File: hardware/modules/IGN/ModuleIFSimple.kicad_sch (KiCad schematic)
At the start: 4 parts, among them J401 Jumper, J402 Conn_01x04_MountingPin

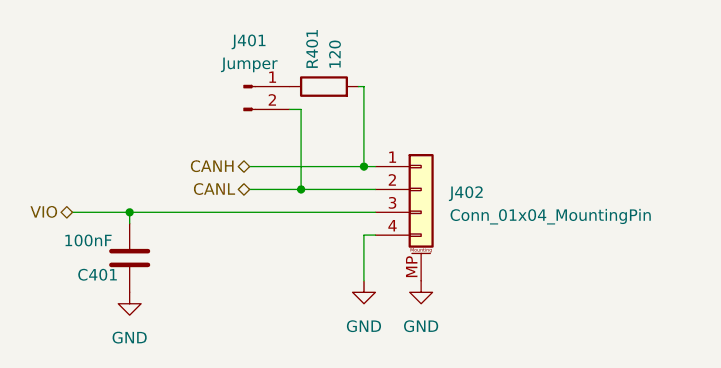
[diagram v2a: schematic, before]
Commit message: CAN周り終端抵抗の位置とか一部変更
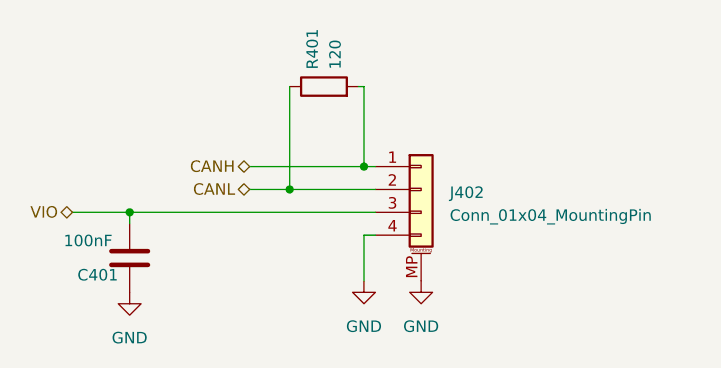
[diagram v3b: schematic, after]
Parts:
- removed J401: Jumper, Connector_PinHeader_1.27mm:PinHeader_1x02_P1.27mm_Vertical, symbol Connector:Conn_01x02_Pin
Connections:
- net CANL: now also R401.1
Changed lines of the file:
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@@
+	)
+	(junction
+		(at 172.72 66.04)
+		(diameter 0)
+		(color 0 0 0 0)
 	)
 	(junction
@@
 		(color 0 0 0 0)
 	)
-	(junction
-		(at 173.99 66.04)
-		(diameter 0)
-		(color 0 0 0 0)
-	)
 	(wire
 		(pts
@@
 	(wire
 		(pts
-			(xy 173.99 57.15) (xy 173.99 66.04)
-		)
-		(stroke
-			(width 0)
-			(type default)
-		)
-	)
-	(wire
-		(pts
 			(xy 154.94 68.58) (xy 182.245 68.58)
 		)
@@
 	(wire
 		(pts
-			(xy 173.99 66.04) (xy 182.245 66.04)
-		)
-		(stroke
-			(width 0)
-			(type default)
-		)
-	)
-	(wire
-		(pts
 			(xy 154.94 68.58) (xy 154.94 69.85)
 		)
@@
 	(wire
 		(pts
+			(xy 172.72 66.04) (xy 182.245 66.04)
+		)
+		(stroke
+			(width 0)
+			(type default)
+		)
+	)
+	(wire
+		(pts
 			(xy 182.245 71.12) (xy 180.975 71.12)
 		)
@@
 	(wire
 		(pts
-			(xy 168.275 66.04) (xy 173.99 66.04)
-		)
-		(stroke
-			(width 0)
-			(type default)
-		)
-	)
-	(wire
-		(pts
-			(xy 172.72 57.15) (xy 173.99 57.15)
+			(xy 172.72 54.61) (xy 172.72 66.04)
+		)
+		(stroke
+			(width 0)
+			(type default)
+		)
+	)
+	(wire
+		(pts
+			(xy 168.275 66.04) (xy 172.72 66.04)
 		)
 		(stroke
@@
 					(unit 1)
 				)
-			)
-		)
-	)
-	(symbol
-		(lib_id "Connector:Conn_01x02_Pin")
-		(at 167.64 54.61 0)
-		(unit 1)
-		(exclude_from_sim no)
-		(in_bom yes)
-		(on_board yes)
-		(dnp no)
-		(fields_autoplaced yes)
-		(property "Reference" "J401"
-			(at 168.275 49.53 0)
-			(effects
-				(font
-					(size 1.27 1.27)
-				)
-			)
-		)
-		(property "Value" "Jumper"
-			(at 168.275 52.07 0)
-			(effects
-				(font
-					(size 1.27 1.27)
-				)
-			)
-		)
-		(property "Footprint" "Connector_PinHeader_1.27mm:PinHeader_1x02_P1.27mm_Vertical"
-			(at 167.64 54.61 0)
-			(effects
-				(font
-					(size 1.27 1.27)
-				)
-				(hide yes)
-			)
-		)
-		(property "Datasheet" "~"
-			(at 167.64 54.61 0)
-			(effects
-				(font
-					(size 1.27 1.27)
-				)
-				(hide yes)
-			)
-		)
-		(property "Description" ""
-			(at 167.64 54.61 0)
-			(effects
-				(font
-					(size 1.27 1.27)
-				)
-				(hide yes)
-			)
-		)
-		(property "LCSC" ""
-			(at 167.64 54.61 0)
-			(effects
-				(font
-					(size 1.27 1.27)
-				)
-				(hide yes)
-			)
-		)
-		(pin "1"
-		)
-		(pin "2"
-		)
-		(instances
-			(project "IGN"
-				(path "/2a7771e6-36a4-47ae-b559-dde705e1d286/0dc43a57-3d63-409f-ae53-b1796098c7d8"
-					(reference "J401")
-					(unit 1)
-				)
-			)
-			(project "GS"
-				(path "/920f9ee9-d8de-4f24-ad72-1c45434a67fe/b6596e6a-331e-4110-9845-3f13c73105a2"
-					(reference "J1")
-					(unit 1)
-				)
-				(path "/920f9ee9-d8de-4f24-ad72-1c45434a67fe/b68d4887-c983-40fc-adcd-c70e88ae0d4a"
-					(reference "J1")
-					(unit 1)
-				)
-			)
-			(project "ModuleIFSimple"
-				(path "/d339b9d8-51a7-460e-bb19-8d8c25d3e2aa"
-					(reference "J101")
-					(unit 1)
-				)
